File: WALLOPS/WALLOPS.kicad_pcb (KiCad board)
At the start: 2 copper layers, 17 parts, among them U9 TPS62147RGXR

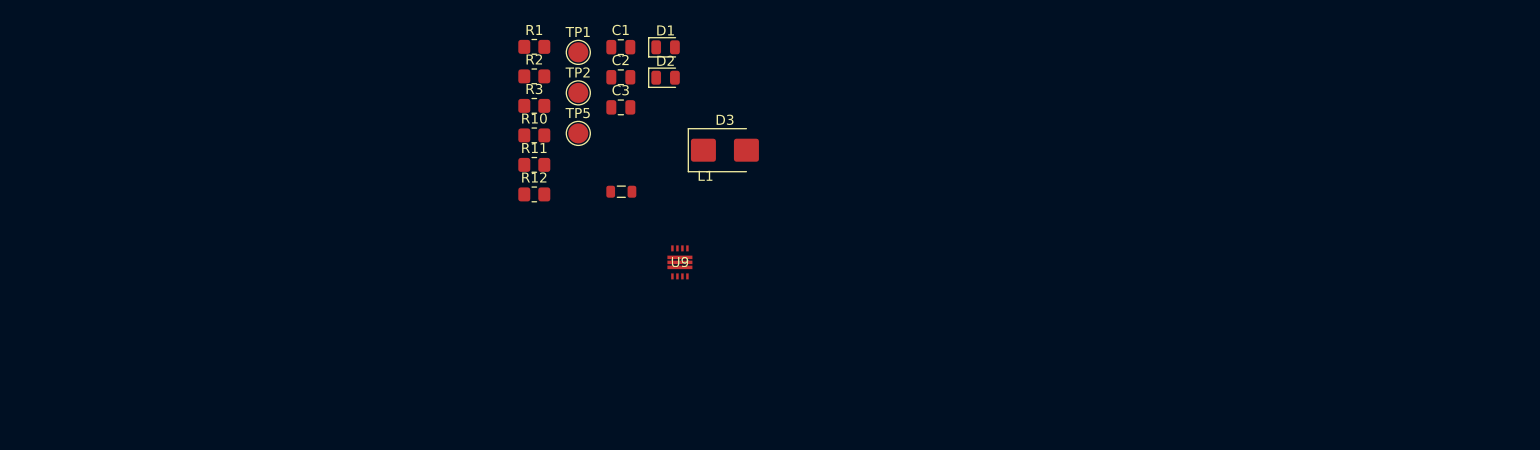
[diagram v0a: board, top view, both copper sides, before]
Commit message: Updated schematic and PCB; added symbol, dimensions, and footprint for Pololu VL53L8CX carrier board
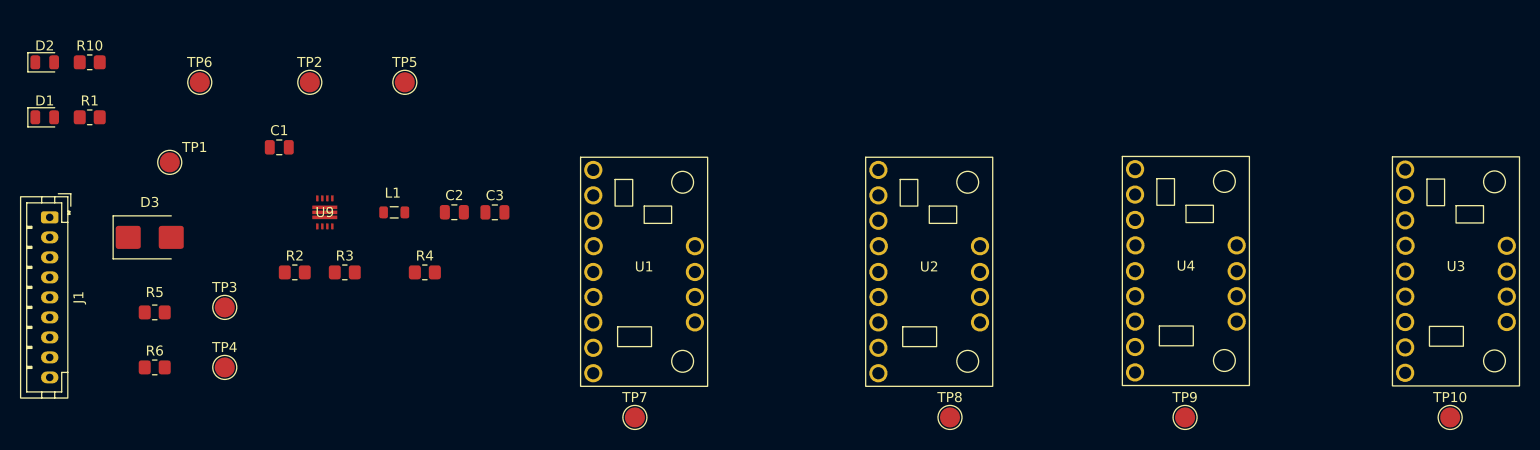
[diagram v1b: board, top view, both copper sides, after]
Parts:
- removed R11, R12: 4.7kΩ, Resistor_SMD:R_0805_2012Metric_Pad1.20x1.40mm_HandSolder
- added J1: JST-PH 1x8 Connector from WALLOPS to ML Suite, Connector_JST:JST_PH_B9B-PH-K_1x09_P2.00mm_Vertical, F.Cu at (51.5, 94.0)
- added R4: 200kΩ, Resistor_SMD:R_0805_2012Metric_Pad1.20x1.40mm_HandSolder, F.Cu at (89.0, 99.5)
- added R5: 2.2kΩ, Resistor_SMD:R_0805_2012Metric_Pad1.20x1.40mm_HandSolder, F.Cu at (62.0, 103.5)
- added R6: 2.2kΩ, Resistor_SMD:R_0805_2012Metric_Pad1.20x1.40mm_HandSolder, F.Cu at (62.0, 109.0)
- added TP10: LPn3_TP, TestPoint:TestPoint_Pad_D2.0mm, F.Cu at (191.5, 114.0)
- added TP3: SCL_Test, TestPoint:TestPoint_Pad_D2.0mm, F.Cu at (69.0, 103.0)
- added TP4: SDA_Test, TestPoint:TestPoint_Pad_D2.0mm, F.Cu at (69.0, 109.0)
- added TP6: GND_TP, TestPoint:TestPoint_Pad_D2.0mm, F.Cu at (66.5, 80.5)
- added TP7: LPn0_TP, TestPoint:TestPoint_Pad_D2.0mm, F.Cu at (110.0, 114.0)
- added TP8: LPn1_TP, TestPoint:TestPoint_Pad_D2.0mm, F.Cu at (141.5, 114.0)
- added TP9: LPn2_TP, TestPoint:TestPoint_Pad_D2.0mm, F.Cu at (165.0, 114.0)
- added U1: VL53L8CX 0 (Zwicky), RockSat:VL53L8CX, F.Cu at (110.9, 99.4)
- added U2: VL58L8CX 1 (Aristotle), RockSat:VL53L8CX, F.Cu at (139.4, 99.4)
- added U3: VL53L8CX 3 (Copernicus), RockSat:VL53L8CX, F.Cu at (192.1, 99.4)
- added U4: VL53L8CX 2 (Brahe), RockSat:VL53L8CX, F.Cu at (165.1, 99.4)
- R10: value 25Ω -> 330Ω
- R2: value 625kΩ -> 620kΩ
- R3: value 200kΩ -> 5.1kΩ
- moved D1 62.5 mm to (51.0, 84.0)
- moved D2 62.1 mm to (51.0, 78.5)
- moved D3 58.2 mm to (61.5, 96.0)
- moved R10 45.0 mm to (55.5, 78.5)
- moved R1 45.0 mm to (55.5, 84.0)
- moved TP1 42.3 mm to (63.5, 88.5)
- moved U9 35.9 mm to (79.0, 93.5)
- moved C1 35.6 mm to (74.5, 87.0)
- moved R2 30.9 mm to (76.0, 99.5)
- moved TP2 26.9 mm to (77.5, 80.5)
- moved R3 25.2 mm to (81.0, 99.5)
- moved L1 22.8 mm to (85.9, 93.5)
- moved C2 21.4 mm to (92.0, 93.5)
- moved TP5 18.1 mm to (87.0, 80.5)
- moved C3 16.4 mm to (96.0, 93.5)
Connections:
- net /3.3V renamed /3.3VOUT
- C1 pad 2: Net-(D3-K) -> /5Vin
- D2 pad 1: Net-(D2-K) -> GND
- D2 pad 2: GND -> Net-(D2-A)
- D3 pad 1: Net-(D3-K) -> /5Vin
- D3 pad 2: 5V -> /5Vin
- R1 pad 2: Net-(D3-K) -> /5Vin
- R10 pad 1: RPi_GPIO -> /SCAN_LED
- R10 pad 2: Net-(D2-K) -> Net-(D2-A)
- R2 pad 2: Net-(U9-FB) -> Net-(R2-Pad2)
- R3 pad 1: Net-(U9-FB) -> Net-(R2-Pad2)
- R3 pad 2: GND -> Net-(U9-FB)
- TP1 pad 1: Net-(D3-K) -> /5Vin
- TP2 pad 1: Net-(D3-K) -> /5Vin
- U9 pad 1: Net-(D3-K) -> /5Vin
- U9 pad 8: Net-(D3-K) -> /5Vin

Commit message: Updated pcb layout and renamed WALLOPS.md to README.md
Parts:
- moved R5 12.3 mm to (66.5, 115.0)
- moved R6 12.3 mm to (66.5, 120.5)
- moved TP3 12.3 mm to (73.5, 114.5)
- moved TP4 12.3 mm to (73.5, 120.5)
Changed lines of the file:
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@@
 	(footprint "TestPoint:TestPoint_Pad_D2.0mm"
 		(layer "F.Cu")
-		(at 69 103)
+		(at 73.5 114.5)
 		(descr "SMD pad as test Point, diameter 2.0mm")
 		(tags "test point SMD pad")
@@
 	(footprint "Resistor_SMD:R_0805_2012Metric_Pad1.20x1.40mm_HandSolder"
 		(layer "F.Cu")
-		(at 62 103.5)
+		(at 66.5 115)
 		(descr "Resistor SMD 0805 (2012 Metric), square (rectangular) end terminal, IPC-7351 nominal with elongated pad for handsoldering. (Body size source: IPC-SM-782 page 72, https://www.pcb-3d.com/wordpress/wp-content/uploads/ipc-sm-782a_amendment_1_and_2.pdf), generated with kicad-footprint-generator")
 		(tags "resistor handsolder")
@@
 	(footprint "TestPoint:TestPoint_Pad_D2.0mm"
 		(layer "F.Cu")
-		(at 69 109)
+		(at 73.5 120.5)
 		(descr "SMD pad as test Point, diameter 2.0mm")
 		(tags "test point SMD pad")
@@
 	(footprint "Resistor_SMD:R_0805_2012Metric_Pad1.20x1.40mm_HandSolder"
 		(layer "F.Cu")
-		(at 62 109)
+		(at 66.5 120.5)
 		(descr "Resistor SMD 0805 (2012 Metric), square (rectangular) end terminal, IPC-7351 nominal with elongated pad for handsoldering. (Body size source: IPC-SM-782 page 72, https://www.pcb-3d.com/wordpress/wp-content/uploads/ipc-sm-782a_amendment_1_and_2.pdf), generated with kicad-footprint-generator")
 		(tags "resistor handsolder")

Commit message: Swapped out sch diode with P-MOSFET to fix backflow on 5VIN
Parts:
- moved D3 1.00 mm to (60.5, 96.0), turned to 180 degrees
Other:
- copper layers 2 -> 4
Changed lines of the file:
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@@
 	(layers
 		(0 "F.Cu" signal)
+		(4 "In1.Cu" signal)
+		(6 "In2.Cu" signal)
 		(2 "B.Cu" signal)
 		(9 "F.Adhes" user "F.Adhesive")
@@
 		(43 "User.3" user)
 		(45 "User.4" user)
+		(47 "User.5" user)
+		(49 "User.6" user)
+		(51 "User.7" user)
+		(53 "User.8" user)
+		(55 "User.9" user)
 	)
 	(setup
+		(stackup
+			(layer "F.SilkS"
+				(type "Top Silk Screen")
+			)
+			(layer "F.Paste"
+				(type "Top Solder Paste")
+			)
+			(layer "F.Mask"
+				(type "Top Solder Mask")
+				(thickness 0.01)
+			)
+			(layer "F.Cu"
+				(type "copper")
+				(thickness 0.035)
+			)
+			(layer "dielectric 1"
+				(type "prepreg")
+				(thickness 0.1)
+				(material "FR4")
+				(epsilon_r 4.5)
+				(loss_tangent 0.02)
+			)
+			(layer "In1.Cu"
+				(type "copper")
+				(thickness 0.035)
+			)
+			(layer "dielectric 2"
+				(type "core")
+				(thickness 1.24)
+				(material "FR4")
+				(epsilon_r 4.5)
+				(loss_tangent 0.02)
+			)
+			(layer "In2.Cu"
+				(type "copper")
+				(thickness 0.035)
+			)
+			(layer "dielectric 3"
+				(type "prepreg")
+				(thickness 0.1)
+				(material "FR4")
+				(epsilon_r 4.5)
+				(loss_tangent 0.02)
+			)
+			(layer "B.Cu"
+				(type "copper")
+				(thickness 0.035)
+			)
+			(layer "B.Mask"
+				(type "Bottom Solder Mask")
+				(thickness 0.01)
+			)
+			(layer "B.Paste"
+				(type "Bottom Solder Paste")
+			)
+			(layer "B.SilkS"
+				(type "Bottom Silk Screen")
+			)
+			(copper_finish "HAL lead-free")
+			(dielectric_constraints no)
+		)
 		(pad_to_mask_clearance 0)
 		(allow_soldermask_bridges_in_footprints no)
@@
 	(footprint "Diode_SMD:D_SMB"
 		(layer "F.Cu")
-		(at 61.5 96)
+		(at 60.5 96 180)
 		(descr "Diode SMB (DO-214AA)")
 		(tags "Diode SMB (DO-214AA)")
@@
 		)
 		(property "Datasheet" "~"
-			(at 0 0 0)
+			(at 0 0 180)
 			(unlocked yes)
 			(layer "F.Fab")
@@
 		)
 		(property "Description" "Schottky diode"
-			(at 0 0 0)
+			(at 0 0 180)
 			(unlocked yes)
 			(layer "F.Fab")
@@
 		(attr smd)
 		(fp_line
+			(start -3.66 2.15)
+			(end 2.15 2.15)
+			(stroke
+				(width 0.12)
+				(type solid)
+			)
+			(layer "F.SilkS")
+		)
+		(fp_line
+			(start -3.66 -2.15)
+			(end 2.15 -2.15)
+			(stroke
+				(width 0.12)
+				(type solid)
+			)
+			(layer "F.SilkS")
+		)
+		(fp_line
 			(start -3.66 -2.15)
 			(end -3.66 2.15)
@@
 		)
 		(fp_line
-			(start -3.66 -2.15)
-			(end 2.15 -2.15)
-			(stroke
-				(width 0.12)
-				(type solid)
-			)
-			(layer "F.SilkS")
-		)
-		(fp_line
-			(start -3.66 2.15)
-			(end 2.15 2.15)
-			(stroke
-				(width 0.12)
-				(type solid)
-			)
-			(layer "F.SilkS")
+			(start 3.65 2.25)
+			(end -3.65 2.25)
+			(stroke
+				(width 0.05)
+				(type solid)
+			)
+			(layer "F.CrtYd")
+		)
+		(fp_line
+			(start 3.65 -2.25)
+			(end 3.65 2.25)
+			(stroke
+				(width 0.05)
+				(type solid)
+			)
+			(layer "F.CrtYd")
+		)
+		(fp_line
+			(start -3.65 2.25)
+			(end -3.65 -2.25)
+			(stroke
+				(width 0.05)
+				(type solid)
+			)
+			(layer "F.CrtYd")
 		)
 		(fp_line
@@
 		)
 		(fp_line
-			(start -3.65 2.25)
-			(end -3.65 -2.25)
-			(stroke
-				(width 0.05)
-				(type solid)
-			)
-			(layer "F.CrtYd")
-		)
-		(fp_line
-			(start 3.65 -2.25)
-			(end 3.65 2.25)
-			(stroke
-				(width 0.05)
-				(type solid)
-			)
-			(layer "F.CrtYd")
-		)
-		(fp_line
-			(start 3.65 2.25)
-			(end -3.65 2.25)
-			(stroke
-				(width 0.05)
-				(type solid)
-			)
-			(layer "F.CrtYd")
+			(start 2.3 2)
+			(end -2.3 2)
+			(stroke
+				(width 0.1)
+				(type solid)
+			)
+			(layer "F.Fab")
+		)
+		(fp_line
+			(start 2.3 -2)
+			(end 2.3 2)
+			(stroke
+				(width 0.1)
+				(type solid)
+			)
+			(layer "F.Fab")
+		)
+		(fp_line
+			(start 2.3 -2)
+			(end -2.3 -2)
+			(stroke
+				(width 0.1)
+				(type solid)
+			)
+			(layer "F.Fab")
+		)
+		(fp_line
+			(start 0.50118 0.75032)
+			(end 0.50118 -0.79908)
+			(stroke
+				(width 0.1)
+				(type solid)
+			)
+			(layer "F.Fab")
+		)
+		(fp_line
+			(start 0.50118 0.00102)
+			(end 1.4994 0.00102)
+			(stroke
+				(width 0.1)
+				(type solid)
+			)
+			(layer "F.Fab")
+		)
+		(fp_line
+			(start -0.64944 0.00102)
+			(end 0.50118 0.75032)
+			(stroke
+				(width 0.1)
+				(type solid)
+			)
+			(layer "F.Fab")
+		)
+		(fp_line
+			(start -0.64944 0.00102)
+			(end 0.50118 -0.79908)
+			(stroke
+				(width 0.1)
+				(type solid)
+			)
+			(layer "F.Fab")
+		)
+		(fp_line
+			(start -0.64944 0.00102)
+			(end -1.55114 0.00102)
+			(stroke
+				(width 0.1)
+				(type solid)
+			)
+			(layer "F.Fab")
+		)
+		(fp_line
+			(start -0.64944 -0.79908)
+			(end -0.64944 0.80112)
+			(stroke
+				(width 0.1)
+				(type solid)
+			)
+			(layer "F.Fab")
 		)
 		(fp_line
@@
 			(layer "F.Fab")
 		)
-		(fp_line
-			(start -0.64944 -0.79908)
-			(end -0.64944 0.80112)
-			(stroke
-				(width 0.1)
-				(type solid)
-			)
-			(layer "F.Fab")
-		)
-		(fp_line
-			(start -0.64944 0.00102)
-			(end -1.55114 0.00102)
-			(stroke
-				(width 0.1)
-				(type solid)
-			)
-			(layer "F.Fab")
-		)
-		(fp_line
-			(start -0.64944 0.00102)
-			(end 0.50118 -0.79908)
-			(stroke
-				(width 0.1)
-				(type solid)
-			)
-			(layer "F.Fab")
-		)
-		(fp_line
-			(start -0.64944 0.00102)
-			(end 0.50118 0.75032)
-			(stroke
-				(width 0.1)
-				(type solid)
-			)
-			(layer "F.Fab")
-		)
-		(fp_line
-			(start 0.50118 0.00102)
-			(end 1.4994 0.00102)
-			(stroke
-				(width 0.1)
-				(type solid)
-			)
-			(layer "F.Fab")
-		)
-		(fp_line
-			(start 0.50118 0.75032)
-			(end 0.50118 -0.79908)
-			(stroke
-				(width 0.1)
-				(type solid)
-			)
-			(layer "F.Fab")
-		)
-		(fp_line
-			(start 2.3 -2)
-			(end -2.3 -2)
-			(stroke
-				(width 0.1)
-				(type solid)
-			)
-			(layer "F.Fab")
-		)
-		(fp_line
-			(start 2.3 -2)
-			(end 2.3 2)
-			(stroke
-				(width 0.1)
-				(type solid)
-			)
-			(layer "F.Fab")
-		)
-		(fp_line
-			(start 2.3 2)
-			(end -2.3 2)
-			(stroke
-				(width 0.1)
-				(type solid)
-			)
-			(layer "F.Fab")
-		)
 		(fp_text user "${REFERENCE}"
 			(at 0 -3.5 0)
@@
 		)
 		(pad "1" smd roundrect
-			(at -2.15 0)
+			(at -2.15 0 180)
 			(size 2.5 2.3)
 			(layers "F.Cu" "F.Mask" "F.Paste")
@@
 		)
 		(pad "2" smd roundrect
-			(at 2.15 0)
+			(at 2.15 0 180)
 			(size 2.5 2.3)
 			(layers "F.Cu" "F.Mask" "F.Paste")

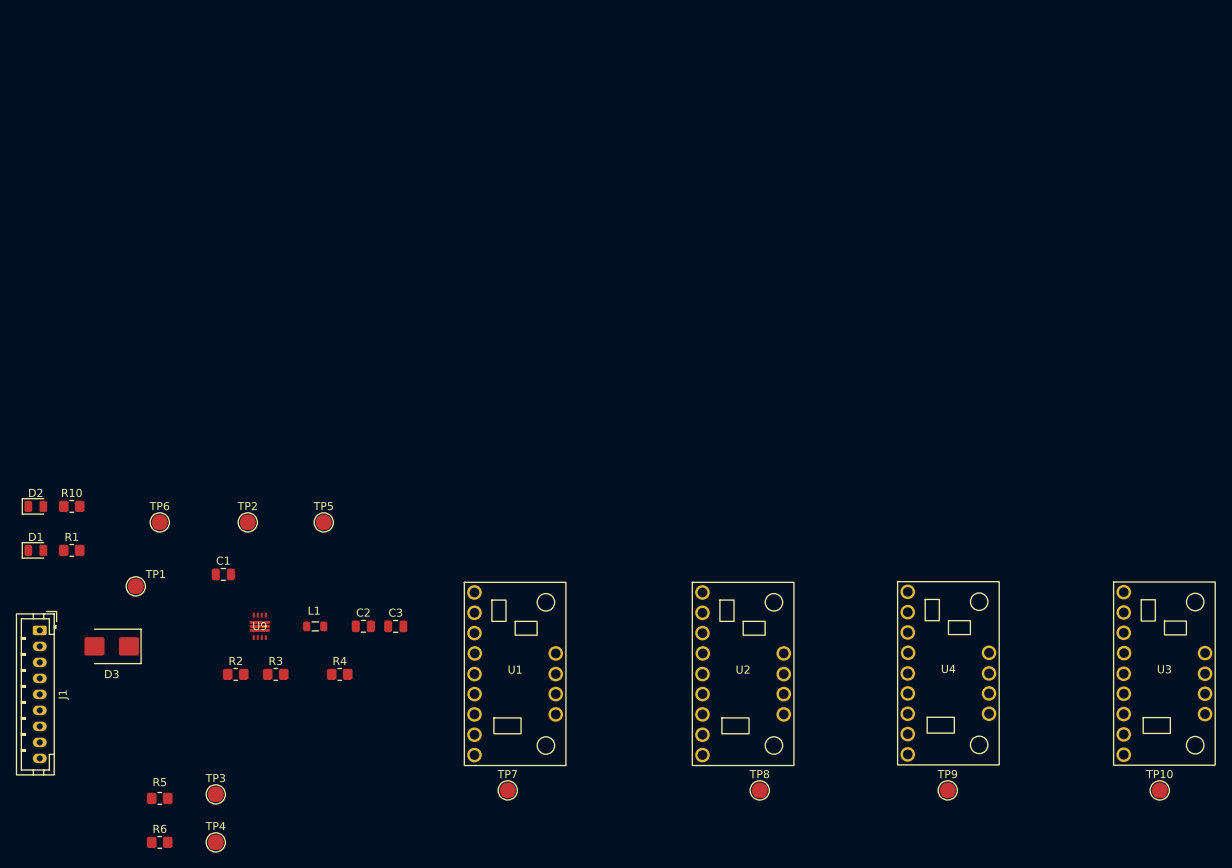
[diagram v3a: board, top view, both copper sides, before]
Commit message: Finished first draft of wallops pcb layout
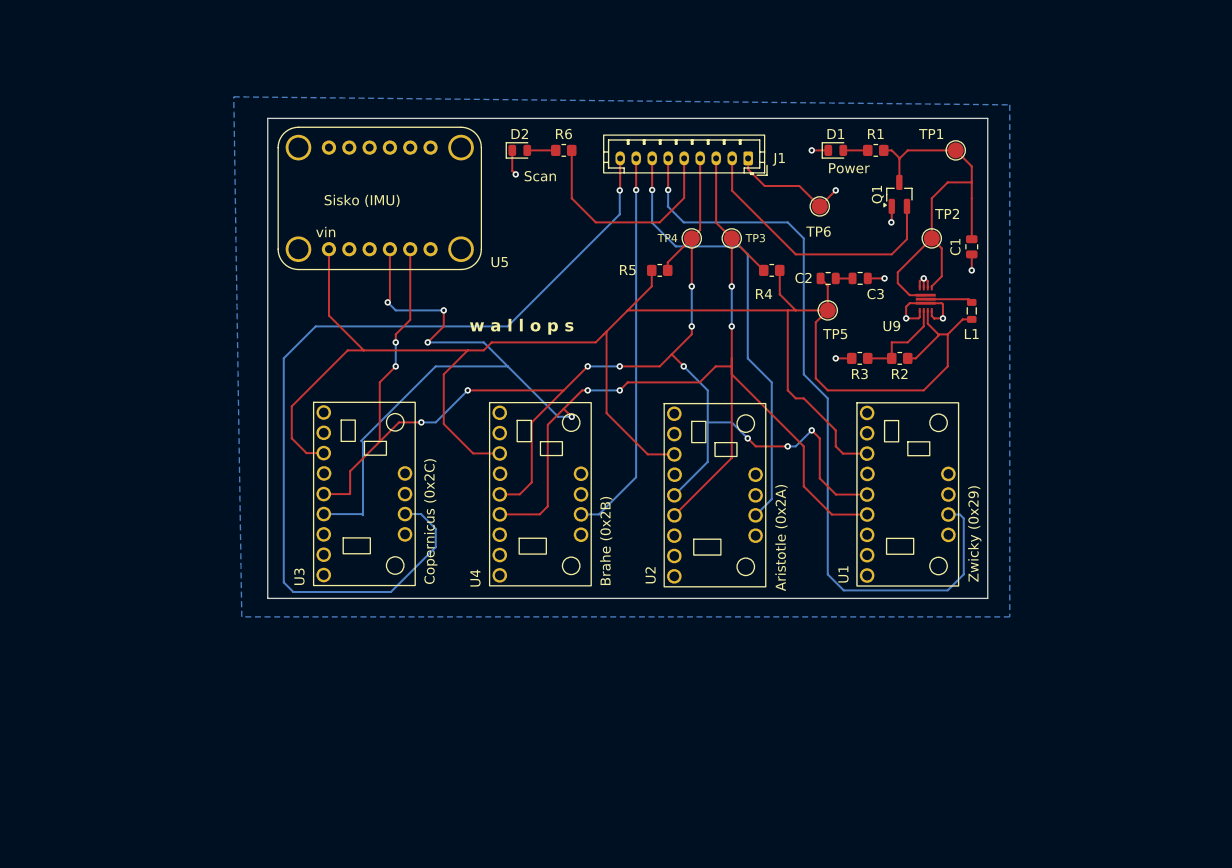
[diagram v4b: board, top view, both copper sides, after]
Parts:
- removed D3: D_Schottky, Diode_SMD:D_SMB
- removed R10: 330Ω, Resistor_SMD:R_0805_2012Metric_Pad1.20x1.40mm_HandSolder
- removed TP10: LPn3_TP, TestPoint:TestPoint_Pad_D2.0mm
- removed TP7: LPn0_TP, TestPoint:TestPoint_Pad_D2.0mm
- removed TP8: LPn1_TP, TestPoint:TestPoint_Pad_D2.0mm
- removed TP9: LPn2_TP, TestPoint:TestPoint_Pad_D2.0mm
- added Q1: AO3401A, Package_TO_SOT_SMD:SOT-23_Handsoldering, F.Cu at (158.9, 39.5)
- added U5: 6DOF IMU (Sisko), RockSat:6DOF IMU, F.Cu at (94.0, 40.0)
- J1: value JST-PH 1x8 Connector from WALLOPS to ML Suite -> JST-PH 1x8 Connector - WALLOPS to ML Suite
- R2: value 620kΩ -> 200kΩ
- R3: value 5.1kΩ -> 620kΩ
- R4: value 200kΩ -> 2.2kΩ
- R6: value 2.2kΩ -> 330Ω
- moved TP1 116.1 mm to (166.0, 34.0)
- moved R1 112.3 mm to (156.0, 34.0)
- moved D1 111.8 mm to (151.0, 34.0)
- moved J1 106.4 mm to (140.1, 35.0), turned to 180 degrees
- moved U3 102.5 mm to (92.1, 76.9)
- moved C1 102.1 mm to (168.0, 46.0), turned to 90 degrees
- moved R6 100.2 mm to (117.0, 34.0), turned to 180 degrees
- moved TP4 96.1 mm to (133.0, 45.0)
- moved TP3 94.8 mm to (138.0, 45.0)
- moved U9 92.8 mm to (162.3, 52.6)
- moved TP2 92.6 mm to (163.0, 45.0)
- moved R2 91.9 mm to (159.0, 60.0), turned to 180 degrees
- moved TP6 91.5 mm to (149.0, 41.0)
- moved L1 91.0 mm to (168.0, 54.1), turned to -90 degrees
- moved R5 90.9 mm to (129.0, 49.0)
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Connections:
- R2 pad 2: Net-(R2-Pad2) -> Net-(U9-FB)
- R3 pad 1: Net-(R2-Pad2) -> Net-(U9-FB)
- R3 pad 2: Net-(U9-FB) -> GND
- R4 pad 1: Net-(U9-FB) -> /SCL
- R4 pad 2: GND -> /3.3VOUT
- R5 pad 1: /SCL -> /3.3VOUT
- R5 pad 2: /3.3VOUT -> /SDA
- R6 pad 1: /3.3VOUT -> /SCAN_LED
- R6 pad 2: /SDA -> Net-(D2-A)
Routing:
- net /3.3VOUT: track 0.00 -> 221.0 mm
- net /SCL: track 0.00 -> 203.6 mm, vias 0 -> 8
- net /SDA: track 0.00 -> 175.4 mm, vias 0 -> 12
- net /LPn_3: track 0.00 -> 113.2 mm, vias 0 -> 1
- net /LPn_0: track 0.00 -> 95.8 mm, vias 0 -> 1
- net /5Vin: track 0.00 -> 88.5 mm
- net /LPn_1: track 0.00 -> 56.4 mm, vias 0 -> 1
- net /LPn_2: track 0.00 -> 48.7 mm, vias 0 -> 1
- net GND: track 0.00 -> 45.6 mm, vias 0 -> 10
- net /SCAN_LED: track 0.00 -> 27.5 mm
- net Net-(U9-FB): track 0.00 -> 11.8 mm
- net Net-(U9-SW): track 0.00 -> 5.92 mm
- net Net-(D2-A): track 0.00 -> 3.56 mm
- net Net-(D1-A): track 0.00 -> 3.06 mm
- net Net-(C2-Pad2): track 0.00 -> 2.10 mm
- added copper zone on B.Cu, net GND
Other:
- board outline added: 90 x 60 mm
- board text added: "Aristotle (0x2A)"
- board text added: "Brahe (0x2B)"
- board text added: "Copernicus (0x2C)"
- board text added: "Power"
- board text added: "Scan"
- board text added: "Sisko (IMU)"
- board text added: "Zwicky (0x29)"
- board text added: "vin"
- board text added: "w a l l o p s"
